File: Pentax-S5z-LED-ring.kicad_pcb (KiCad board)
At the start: 2 copper layers, 40 x 40 mm, 45 parts, among them IC1 ATTINY13-S, P1 CONN_2, P2 +, P3 -, P4 CONN_2, Q1 MOSFET_N, SW1 SW_PUSH, SW2 SW_PUSH

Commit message: Note: add a capacitor.
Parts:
- IC1: footprint MADW__SO8_200mil_wide -> -SOIC8
- moved R17 16.7 mm to (58.5, 67.1), turned to 90 degrees
- moved Q1 15.4 mm to (58.7, 62.5), turned to 90 degrees
- moved SW1 12.0 mm to (69.7, 57.6), turned to 335 degrees
- moved IC1 11.4 mm to (70.3, 65.0), turned to 180 degrees
- moved R18 10.3 mm to (63.8, 62.5), turned to 0 degrees
- moved P1 9.05 mm to (75.0, 65.0), turned to 270 degrees
- moved P4 8.88 mm to (55.0, 65.0), turned to 90 degrees
- moved SW2 8.60 mm to (60.4, 57.6), turned to 205 degrees
- moved JP1 4.42 mm to (63.8, 67.1), turned to 0 degrees
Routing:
- net GND: track 0.00 -> 32.4 mm
- net +5V: track 0.00 -> 31.6 mm, vias 0 -> 2
- net /SCK: track 0.00 -> 27.8 mm, vias 0 -> 4
- net /MISO: track 0.00 -> 26.2 mm, vias 0 -> 2
- net /PWM: track 0.00 -> 17.6 mm, vias 0 -> 1
- net /RESET: track 0.00 -> 10.4 mm, vias 0 -> 1
- net N-000001: track 0.00 -> 6.65 mm
- net N-0000010: track 0.00 -> 3.04 mm
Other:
- outline, holes or cut-outs redrawn
- board text added: "+5V"
- board text added: "-"
- board text added: "A+"
- board text added: "B-"

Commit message: Getting there...
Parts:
- added C1: 4.7µF, MADW__C0805, F.Cu at (65.0, 62.9)
- moved R18 3.00 mm to (65.0, 59.8)
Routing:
- net +5V: track 31.6 -> 36.7 mm, vias 2 -> 3
- net N-000001: track 6.65 -> 10.4 mm
- net GND: track 32.4 -> 34.0 mm

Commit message: Logos...
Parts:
- added G***: OSHW-logo_silkscreen_4mm, OSHW-logo_silkscreen_4mm, B.Cu at (60.4, 57.6)
- added G***: LED_smile_silkscreen_4mm, LED_smile_silkscreen_4mm, B.Cu at (69.7, 57.6)
- added G***: LED_smile_silkscreen_4mm, LED_smile_silkscreen_4mm, B.Cu at (78.8, 56.0)
- added G***: OSHW-logo_silkscreen_4mm, OSHW-logo_silkscreen_4mm, B.Cu at (50.8, 56.0)
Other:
- board text added: "2013"
- board text added: "blog.spitzenpfeil.org"

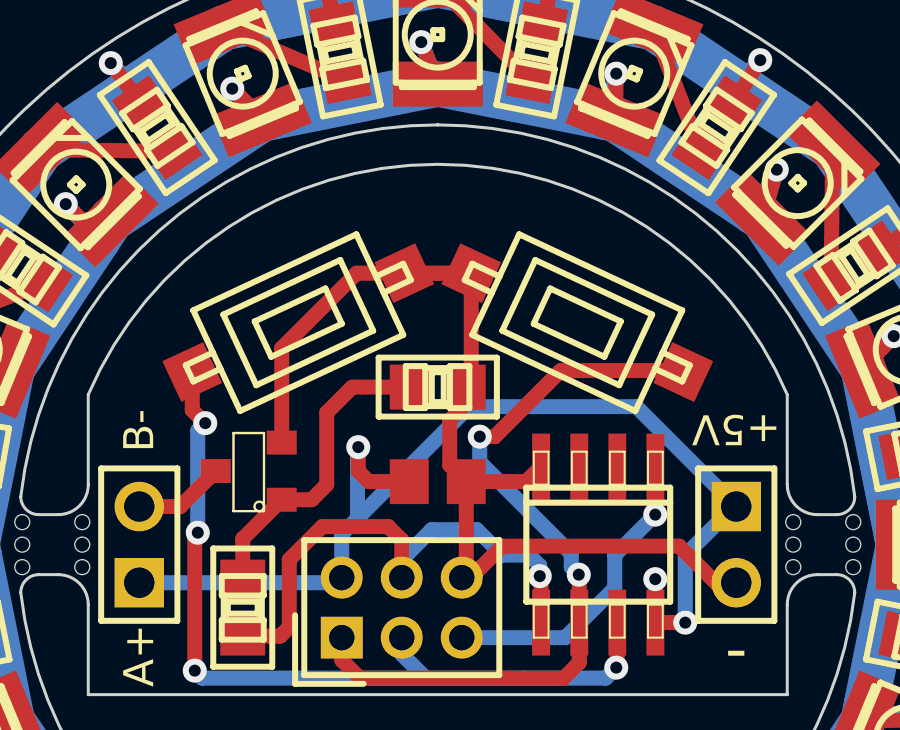
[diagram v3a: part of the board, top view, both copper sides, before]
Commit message: Added 1k resistors for the pull-down switches. Just in case ;-)
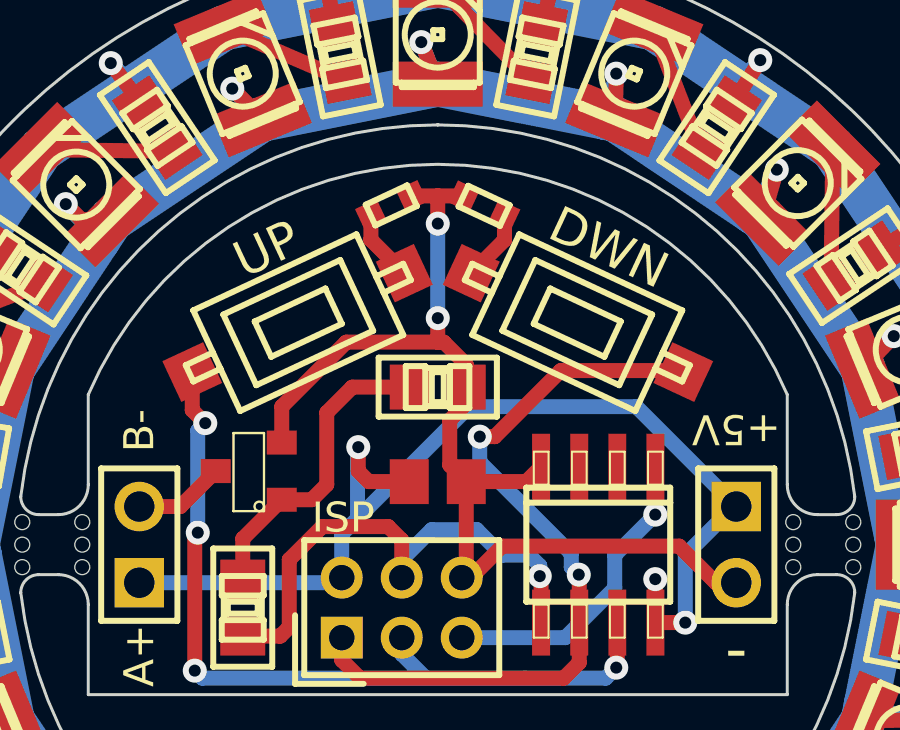
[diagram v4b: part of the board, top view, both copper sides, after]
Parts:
- added R19: 1k, MADW__R0603, F.Cu at (66.5, 53.7)
- added R20: 1k, MADW__R0603, F.Cu at (63.5, 53.7)
- moved G*** 1.15 mm to (60.0, 56.5)
- moved G*** 1.15 mm to (70.0, 56.5)
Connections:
- SW1 pad 1: GND -> N-000002
- SW2 pad 1: GND -> N-0000011
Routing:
- net N-000002: track 0.00 -> 2.77 mm
- net N-0000011: track 0.00 -> 2.74 mm
- net GND: track 34.0 -> 35.8 mm, vias 0 -> 2
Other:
- board text added: "DWN"
- board text added: "UP"
- board text added: "V1.0"
- board text added: "V1.0 2013"

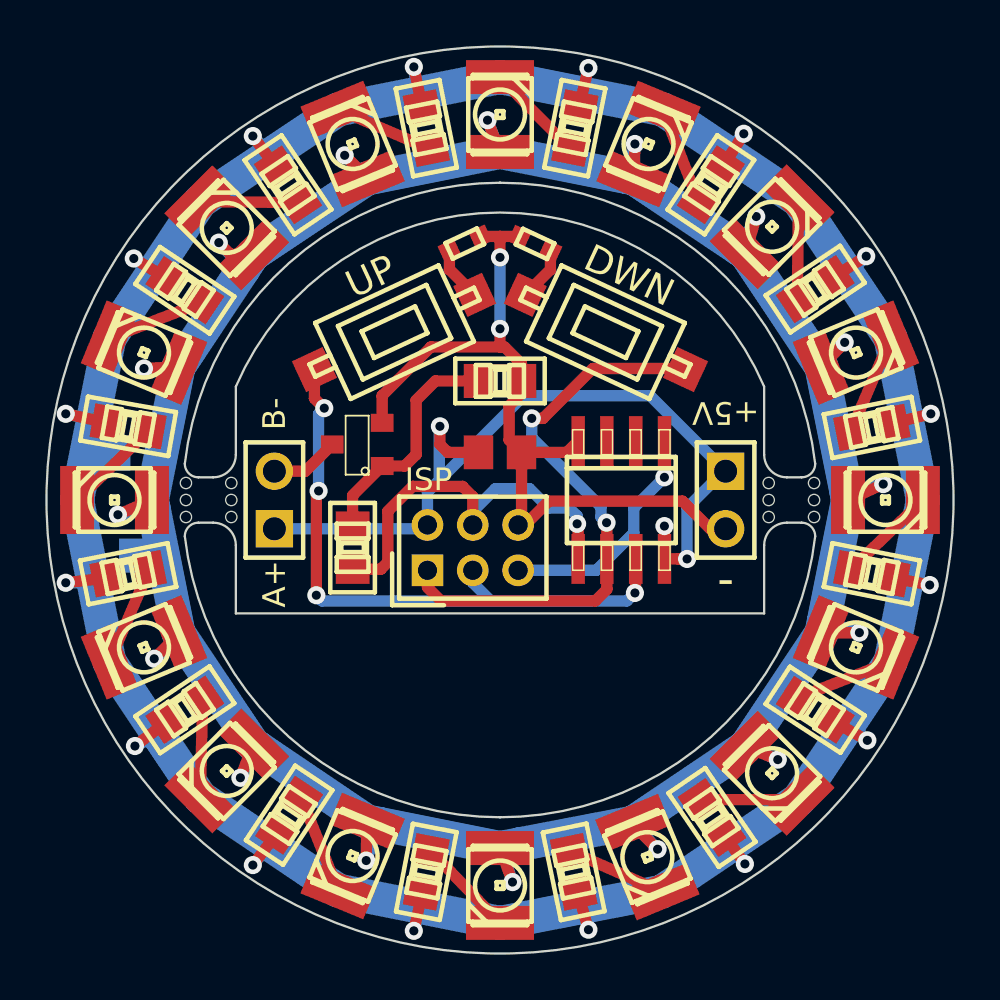
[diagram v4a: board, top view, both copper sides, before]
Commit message: Had to redo the internal cutout. OSHPARK uses a 100mil router, not 0.8mm
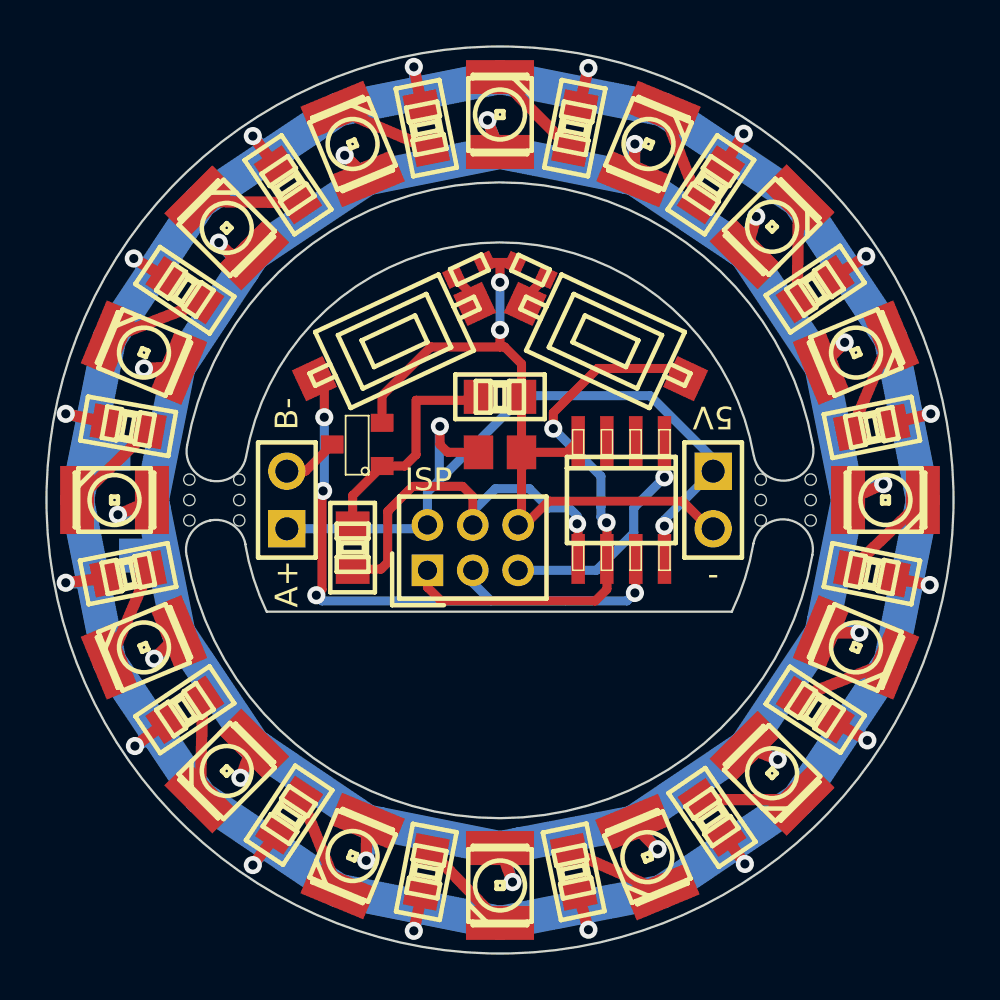
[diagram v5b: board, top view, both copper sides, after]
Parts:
- removed the mouse-bite-2mm at (78.1, 65.0)
- removed the mouse-bite-2mm at (51.9, 65.0)
- added mouse-bite-2mm: VAL**, MADW__mouse-bite-2mm-slot, F.Cu at (52.4, 65.0)
- added mouse-bite-2mm: VAL**, MADW__mouse-bite-2mm-slot, F.Cu at (77.6, 65.0)
- moved G*** 6.78 mm to (69.7, 63.3)
- moved G*** 6.78 mm to (59.8, 63.3)
- moved R19 1.17 mm to (66.3, 54.9)
- moved R20 1.17 mm to (63.6, 54.9)
- moved R18 0.70 mm to (65.0, 60.5)
- moved P4 0.55 mm to (55.6, 65.0)
- moved P1 0.55 mm to (74.4, 65.0)
- moved SW1 0.40 mm to (69.7, 58.0)
- moved SW2 0.40 mm to (60.4, 58.0)
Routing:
- net +5V: track 36.7 -> 34.1 mm, vias 3 -> 2
- net GND: track 35.8 -> 33.6 mm
- net N-000002: track 2.77 -> 1.56 mm
- net /MISO: track 25.8 -> 24.6 mm
- net N-0000011: track 2.74 -> 1.57 mm
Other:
- outline, holes or cut-outs redrawn
- net class Default: trace_width 0.5 -> 0.4
- board text added: "5V"
- board text added: "blog. spitzenpfeil.org"
- board text removed: "+5V"
- board text removed: "DWN"
- board text removed: "UP"

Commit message: Changed the LED dropper resistors to 65R + added some text.
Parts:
- R1: value 60R -> 65R
- R10, R11, R12, R13, R14, R15, R16, R2, R3, R4, R5, R6, R7, R8, R9: value 10R -> 65R
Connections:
- IC1 pad 2: (no net) -> N-000006
- IC1 pad 3: (no net) -> N-000005
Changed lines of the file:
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@@
-(kicad_pcb (version 3) (host pcbnew "(2013-04-07 BZR 4075)-testing")
+(kicad_pcb (version 3) (host pcbnew "(2013-04-28 BZR 4116)-testing")
   (general
     (links 71)
@@
     (zones 0)
     (modules 52)
-    (nets 29)
+    (nets 31)
   )
   (page User 431.8 279.4)
@@
   (net 25 N-0000029)
   (net 26 N-0000030)
-  (net 27 N-000008)
-  (net 28 N-000009)
+  (net 27 N-000005)
+  (net 28 N-000006)
+  (net 29 N-000008)
+  (net 30 N-000009)
   (net_class Default "This is the default net class."
     (clearance 0.25)
@@
     (add_net N-0000029)
     (add_net N-0000030)
+    (add_net N-000005)
+    (add_net N-000006)
     (add_net N-000008)
     (add_net N-000009)
@@
       (effects (font (size 1 1) (thickness 0.2)))
     )
-    (fp_text value 10R (at 0 1.9 101.3) (layer F.SilkS) hide
+    (fp_text value 65R (at 0 1.9 101.3) (layer F.SilkS) hide
       (effects (font (size 1 1) (thickness 0.2)))
     )
@@
       (effects (font (size 1 1) (thickness 0.2)))
     )
-    (fp_text value 10R (at 0 1.9 123.9) (layer F.SilkS) hide
+    (fp_text value 65R (at 0 1.9 123.9) (layer F.SilkS) hide
       (effects (font (size 1 1) (thickness 0.2)))
     )
@@
       (effects (font (size 1 1) (thickness 0.2)))
     )
-    (fp_text value 10R (at 0 1.9 146.3) (layer F.SilkS) hide
+    (fp_text value 65R (at 0 1.9 146.3) (layer F.SilkS) hide
       (effects (font (size 1 1) (thickness 0.2)))
     )
@@
       (effects (font (size 1 1) (thickness 0.2)))
     )
-    (fp_text value 10R (at 0 1.9 170) (layer F.SilkS) hide
+    (fp_text value 65R (at 0 1.9 170) (layer F.SilkS) hide
       (effects (font (size 1 1) (thickness 0.2)))
     )
@@
       (effects (font (size 1 1) (thickness 0.2)))
     )
-    (fp_text value 10R (at 0 1.9 191.3) (layer F.SilkS) hide
+    (fp_text value 65R (at 0 1.9 191.3) (layer F.SilkS) hide
       (effects (font (size 1 1) (thickness 0.2)))
     )
@@
       (effects (font (size 1 1) (thickness 0.2)))
     )
-    (fp_text value 10R (at 0 1.9 213.9) (layer F.SilkS) hide
+    (fp_text value 65R (at 0 1.9 213.9) (layer F.SilkS) hide
       (effects (font (size 1 1) (thickness 0.2)))
     )
@@
       (effects (font (size 1 1) (thickness 0.2)))
     )
-    (fp_text value 10R (at 0 1.9 236.5) (layer F.SilkS) hide
+    (fp_text value 65R (at 0 1.9 236.5) (layer F.SilkS) hide
       (effects (font (size 1 1) (thickness 0.2)))
     )
@@
       (effects (font (size 1 1) (thickness 0.2)))
     )
-    (fp_text value 10R (at 0 1.9 259.1) (layer F.SilkS) hide
+    (fp_text value 65R (at 0 1.9 259.1) (layer F.SilkS) hide
       (effects (font (size 1 1) (thickness 0.2)))
     )
@@
       (effects (font (size 1 1) (thickness 0.2)))
     )
-    (fp_text value 10R (at 0 1.9 281.7) (layer F.SilkS) hide
+    (fp_text value 65R (at 0 1.9 281.7) (layer F.SilkS) hide
       (effects (font (size 1 1) (thickness 0.2)))
     )
@@
       (effects (font (size 1 1) (thickness 0.2)))
     )
-    (fp_text value 10R (at 0 1.9 304.3) (layer F.SilkS) hide
+    (fp_text value 65R (at 0 1.9 304.3) (layer F.SilkS) hide
       (effects (font (size 1 1) (thickness 0.2)))
     )
@@
       (effects (font (size 1 1) (thickness 0.2)))
     )
-    (fp_text value 10R (at 0 1.9 326.9) (layer F.SilkS) hide
+    (fp_text value 65R (at 0 1.9 326.9) (layer F.SilkS) hide
       (effects (font (size 1 1) (thickness 0.2)))
     )
@@
       (effects (font (size 1 1) (thickness 0.2)))
     )
-    (fp_text value 60R (at 0 1.9 78.7) (layer F.SilkS) hide
+    (fp_text value 65R (at 0 1.9 78.7) (layer F.SilkS) hide
       (effects (font (size 1 1) (thickness 0.2)))
     )
@@
       (effects (font (size 1 1) (thickness 0.2)))
     )
-    (fp_text value 10R (at 0 1.9 11.3) (layer F.SilkS) hide
+    (fp_text value 65R (at 0 1.9 11.3) (layer F.SilkS) hide
       (effects (font (size 1 1) (thickness 0.2)))
     )
@@
       (effects (font (size 1 1) (thickness 0.2)))
     )
-    (fp_text value 10R (at 0 1.9 56.3) (layer F.SilkS) hide
+    (fp_text value 65R (at 0 1.9 56.3) (layer F.SilkS) hide
       (effects (font (size 1 1) (thickness 0.2)))
     )
@@
       (effects (font (size 1 1) (thickness 0.2)))
     )
-    (fp_text value 10R (at 0 1.9 33.7) (layer F.SilkS) hide
+    (fp_text value 65R (at 0 1.9 33.7) (layer F.SilkS) hide
       (effects (font (size 1 1) (thickness 0.2)))
     )
@@
       (effects (font (size 1 1) (thickness 0.2)))
     )
-    (fp_text value 10R (at 0 1.9 348.7) (layer F.SilkS) hide
+    (fp_text value 65R (at 0 1.9 348.7) (layer F.SilkS) hide
       (effects (font (size 1 1) (thickness 0.2)))
     )
@@
     (pad 3 smd rect (at 0 -1.09982 90) (size 0.8001 1.00076)
       (layers F.Cu F.Mask)
-      (net 28 N-000009)
+      (net 30 N-000009)
     )
     (pad 2 smd rect (at 0.9525 1.09982 90) (size 0.8001 1.00076)
@@
     (pad 1 smd rect (at -0.9525 1.09982 90) (size 0.8001 1.00076)
       (layers F.Cu F.Mask)
-      (net 27 N-000008)
+      (net 29 N-000008)
     )
     (model smd\SOT23_3.wrl
@@
     (pad 2 smd rect (at 0.94996 0 90) (size 1.29794 1.4986)
       (layers F.Cu F.Mask)
-      (net 27 N-000008)
+      (net 29 N-000008)
     )
   )
@@
     (pad 1 smd rect (at -0.94996 0) (size 1.29794 1.4986)
       (layers F.Cu F.Mask)
-      (net 27 N-000008)
+      (net 29 N-000008)
     )
     (pad 2 smd rect (at 0.94996 0) (size 1.29794 1.4986)
@@
     (pad 2 thru_hole circle (at 1.27 0 90) (size 1.65 1.65) (drill 1.016)
       (layers *.Cu *.Mask F.SilkS)
-      (net 28 N-000009)
+      (net 30 N-000009)
     )
   )
@@
     (pad 2 smd rect (at -0.635 2.59842 180) (size 0.59944 2.19964)
       (layers F.Cu F.Mask)
+      (net 28 N-000006)
     )
     (pad 3 smd rect (at 0.635 2.59842 180) (size 0.59944 2.19964)
       (layers F.Cu F.Mask)
+      (net 27 N-000005)
     )
     (pad 4 smd rect (at 1.905 2.59842 180) (size 0.59944 2.19964)
@@
   (segment (start 73.814673 78.21524) (end 78.166726 78.216726) (width 0.5) (layer F.Cu) (net 25) (status 30))
   (segment (start 68.05736 80.469777) (end 72.131428 82.274401) (width 0.5) (layer F.Cu) (net 26) (status 30))
-  (segment (start 61.3 60.6) (end 63.90004 60.6) (width 0.4) (layer F.Cu) (net 27))
-  (segment (start 61.3 63) (end 60.7975 63.5025) (width 0.4) (layer F.Cu) (net 27))
-  (segment (start 59.79982 63.5025) (end 60.7975 63.5025) (width 0.4) (layer F.Cu) (net 27))
-  (segment (start 61.3 63) (end 61.3 60.6) (width 0.4) (layer F.Cu) (net 27))
-  (segment (start 63.90004 60.6) (end 64.05004 60.45) (width 0.4) (layer F.Cu) (net 27))
-  (segment (start 58.5 66.15004) (end 58.5 64.80232) (width 0.4) (layer F.Cu) (net 27))
-  (segment (start 58.5 64.80232) (end 59.79982 63.5025) (width 0.4) (layer F.Cu) (net 27))
-  (segment (start 55.05 63.73) (end 56.42018 63.73) (width 0.4) (layer F.Cu) (net 28))
-  (segment (start 56.42018 63.73) (end 57.60018 62.55) (width 0.4) (layer F.Cu) (net 28))
+  (segment (start 61.3 60.6) (end 63.90004 60.6) (width 0.4) (layer F.Cu) (net 29))
+  (segment (start 61.3 63) (end 60.7975 63.5025) (width 0.4) (layer F.Cu) (net 29))
+  (segment (start 59.79982 63.5025) (end 60.7975 63.5025) (width 0.4) (layer F.Cu) (net 29))
+  (segment (start 61.3 63) (end 61.3 60.6) (width 0.4) (layer F.Cu) (net 29))
+  (segment (start 63.90004 60.6) (end 64.05004 60.45) (width 0.4) (layer F.Cu) (net 29))
+  (segment (start 58.5 66.15004) (end 58.5 64.80232) (width 0.4) (layer F.Cu) (net 29))
+  (segment (start 58.5 64.80232) (end 59.79982 63.5025) (width 0.4) (layer F.Cu) (net 29))
+  (segment (start 55.05 63.73) (end 56.42018 63.73) (width 0.4) (layer F.Cu) (net 30))
+  (segment (start 56.42018 63.73) (end 57.60018 62.55) (width 0.4) (layer F.Cu) (net 30))
 )

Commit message: 68R it is.
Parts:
- R1, R10, R11, R12, R13, R14, R15, R16, R2, R3, R4, R5, R6, R7, R8, R9: value 65R -> 68R
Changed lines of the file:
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@@
     (links 71)
     (no_connects 0)
-    (area 44.422949 44.422949 85.577051 85.577051)
+    (area 44.949999 44.949999 85.050001 85.050001)
     (thickness 1.6)
     (drawings 26)
@@
       (effects (font (size 1 1) (thickness 0.2)))
     )
-    (fp_text value 65R (at 0 1.9 101.3) (layer F.SilkS) hide
+    (fp_text value 68R (at 0 1.9 101.3) (layer F.SilkS) hide
       (effects (font (size 1 1) (thickness 0.2)))
     )
@@
       (effects (font (size 1 1) (thickness 0.2)))
     )
-    (fp_text value 65R (at 0 1.9 123.9) (layer F.SilkS) hide
+    (fp_text value 68R (at 0 1.9 123.9) (layer F.SilkS) hide
       (effects (font (size 1 1) (thickness 0.2)))
     )
@@
       (effects (font (size 1 1) (thickness 0.2)))
     )
-    (fp_text value 65R (at 0 1.9 146.3) (layer F.SilkS) hide
+    (fp_text value 68R (at 0 1.9 146.3) (layer F.SilkS) hide
       (effects (font (size 1 1) (thickness 0.2)))
     )
@@
       (effects (font (size 1 1) (thickness 0.2)))
     )
-    (fp_text value 65R (at 0 1.9 170) (layer F.SilkS) hide
+    (fp_text value 68R (at 0 1.9 170) (layer F.SilkS) hide
       (effects (font (size 1 1) (thickness 0.2)))
     )
@@
       (effects (font (size 1 1) (thickness 0.2)))
     )
-    (fp_text value 65R (at 0 1.9 191.3) (layer F.SilkS) hide
+    (fp_text value 68R (at 0 1.9 191.3) (layer F.SilkS) hide
       (effects (font (size 1 1) (thickness 0.2)))
     )
@@
       (effects (font (size 1 1) (thickness 0.2)))
     )
-    (fp_text value 65R (at 0 1.9 213.9) (layer F.SilkS) hide
+    (fp_text value 68R (at 0 1.9 213.9) (layer F.SilkS) hide
       (effects (font (size 1 1) (thickness 0.2)))
     )
@@
       (effects (font (size 1 1) (thickness 0.2)))
     )
-    (fp_text value 65R (at 0 1.9 236.5) (layer F.SilkS) hide
+    (fp_text value 68R (at 0 1.9 236.5) (layer F.SilkS) hide
       (effects (font (size 1 1) (thickness 0.2)))
     )
@@
       (effects (font (size 1 1) (thickness 0.2)))
     )
-    (fp_text value 65R (at 0 1.9 259.1) (layer F.SilkS) hide
+    (fp_text value 68R (at 0 1.9 259.1) (layer F.SilkS) hide
       (effects (font (size 1 1) (thickness 0.2)))
     )
@@
       (effects (font (size 1 1) (thickness 0.2)))
     )
-    (fp_text value 65R (at 0 1.9 281.7) (layer F.SilkS) hide
+    (fp_text value 68R (at 0 1.9 281.7) (layer F.SilkS) hide
       (effects (font (size 1 1) (thickness 0.2)))
     )
@@
       (effects (font (size 1 1) (thickness 0.2)))
     )
-    (fp_text value 65R (at 0 1.9 304.3) (layer F.SilkS) hide
+    (fp_text value 68R (at 0 1.9 304.3) (layer F.SilkS) hide
       (effects (font (size 1 1) (thickness 0.2)))
     )
@@
       (effects (font (size 1 1) (thickness 0.2)))
     )
-    (fp_text value 65R (at 0 1.9 326.9) (layer F.SilkS) hide
+    (fp_text value 68R (at 0 1.9 326.9) (layer F.SilkS) hide
       (effects (font (size 1 1) (thickness 0.2)))
     )
@@
       (effects (font (size 1 1) (thickness 0.2)))
     )
-    (fp_text value 65R (at 0 1.9 78.7) (layer F.SilkS) hide
+    (fp_text value 68R (at 0 1.9 78.7) (layer F.SilkS) hide
       (effects (font (size 1 1) (thickness 0.2)))
     )
@@
       (effects (font (size 1 1) (thickness 0.2)))
     )
-    (fp_text value 65R (at 0 1.9 11.3) (layer F.SilkS) hide
+    (fp_text value 68R (at 0 1.9 11.3) (layer F.SilkS) hide
       (effects (font (size 1 1) (thickness 0.2)))
     )
@@
       (effects (font (size 1 1) (thickness 0.2)))
     )
-    (fp_text value 65R (at 0 1.9 56.3) (layer F.SilkS) hide
+    (fp_text value 68R (at 0 1.9 56.3) (layer F.SilkS) hide
       (effects (font (size 1 1) (thickness 0.2)))
     )
@@
       (effects (font (size 1 1) (thickness 0.2)))
     )
-    (fp_text value 65R (at 0 1.9 33.7) (layer F.SilkS) hide
+    (fp_text value 68R (at 0 1.9 33.7) (layer F.SilkS) hide
       (effects (font (size 1 1) (thickness 0.2)))
     )
@@
       (effects (font (size 1 1) (thickness 0.2)))
     )
-    (fp_text value 65R (at 0 1.9 348.7) (layer F.SilkS) hide
-      (effects (font (size 1 1) (thickness 0.2)))
-    )
+    (fp_text value 68R (at 0 1.9 348.7) (layer F.SilkS) hide
+      (effects (font (size 1 1) (thickness 0.2)))
+    )
